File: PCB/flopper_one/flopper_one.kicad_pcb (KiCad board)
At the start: 2 copper layers, 77 x 63 mm, 21 parts, among them J1 To PN532 ->, J2 <- ST7789, Q1 2N2219, SW1 SW_Omron_B3FS, SW2 SW_Omron_B3FS, SW3 SW_Omron_B3FS, SW4 SW_Omron_B3FS, SW5 SW_Omron_B3FS, U1 TP4056-42-ESOP8, U4 hw-045

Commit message: clean stuff up
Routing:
- net GND: track 332.5 -> 362.7 mm, vias 1 -> 0
- net /BAT+: track 33.6 -> 25.7 mm
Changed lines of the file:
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@@
 		(at 169.805 107.7 -90)
 		(property "Reference" "U2"
-			(at -11.355 -27.36 90)
+			(at 0 0 180)
 			(layer "F.SilkS")
 			(effects
@@
 	)
 	(gr_rect
-		(start 197.375 81.3125)
-		(end 199.625 83.6875)
+		(start 197.5 81.25)
+		(end 199.75 83.75)
 		(stroke
-			(width 0.1)
+			(width 0.2)
 			(type solid)
 		)
 		(fill yes)
 		(layer "B.Cu")
+		(net 3)
+	)
+	(gr_rect
+		(start 193.125 81.25)
+		(end 195.375 83.625)
+		(stroke
+			(width 0.2)
+			(type default)
+		)
+		(fill no)
+		(layer "B.Cu")
 		(net 39)
 	)
@@
 	)
 	(gr_text "ESP HERE"
-		(at 164 105 0)
+		(at 165.25 105 0)
 		(layer "F.SilkS")
 		(effects
@@
 	)
 	(segment
+		(start 192.75 106)
+		(end 196.375 102.375)
+		(width 0.2)
+		(layer "F.Cu")
+		(net 3)
+	)
+	(segment
 		(start 202.865 95.19)
 		(end 204.075 95.19)
@@
 	)
 	(segment
-		(start 197.25 103.25)
+		(start 196.375 102.375)
 		(end 192 98)
 		(width 0.2)
@@
 	)
 	(segment
+		(start 196.5 102.5)
+		(end 196.375 102.375)
+		(width 0.2)
+		(layer "F.Cu")
+		(net 3)
+	)
+	(segment
 		(start 209 63)
 		(end 208 62)
@@
 	)
 	(segment
-		(start 205 81)
-		(end 204.25 81)
+		(start 196.5 102.5)
+		(end 197.38 102.5)
 		(width 0.2)
 		(layer "F.Cu")
@@
 	)
 	(segment
-		(start 206 89.25)
-		(end 208 87.25)
+		(start 197.38 102.5)
+		(end 197.69 102.81)
+		(width 0.2)
+		(layer "F.Cu")
+		(net 3)
+	)
+	(segment
+		(start 205 81)
+		(end 204.25 81)
 		(width 0.2)
 		(layer "F.Cu")
@@
 	)
 	(segment
-		(start 195.5 103.25)
-		(end 197.25 103.25)
+		(start 206 89.25)
+		(end 208 87.25)
 		(width 0.2)
 		(layer "F.Cu")
@@
 	)
 	(segment
-		(start 206 89.25)
-		(end 206 87.75)
-		(width 0.2)
-		(layer "F.Cu")
-		(net 3)
-	)
-	(segment
 		(start 200.9 97.025)
 		(end 202.3 97.025)
@@
 	)
 	(segment
-		(start 197.25 103.25)
-		(end 197.69 102.81)
-		(width 0.2)
-		(layer "F.Cu")
-		(net 3)
-	)
-	(segment
 		(start 149.221108 121.701)
 		(end 148.459 120.938892)
@@
 	)
 	(segment
-		(start 192.75 106)
-		(end 195.5 103.25)
-		(width 0.2)
-		(layer "F.Cu")
-		(net 3)
-	)
-	(segment
 		(start 152.3 120.4)
 		(end 150.999 121.701)
@@
 		(net 3)
 	)
-	(via
-		(at 206 87.75)
-		(size 0.6)
-		(drill 0.3)
-		(layers "F.Cu" "B.Cu")
+	(segment
+		(start 208.05 88.75)
+		(end 204.899 91.901)
+		(width 0.2)
+		(layer "B.Cu")
 		(net 3)
 	)
@@
 	)
 	(segment
+		(start 211.210057 102.81)
+		(end 216.25 102.81)
+		(width 0.2)
+		(layer "B.Cu")
+		(net 3)
+	)
+	(segment
+		(start 204.899 96.498943)
+		(end 211.210057 102.81)
+		(width 0.2)
+		(layer "B.Cu")
+		(net 3)
+	)
+	(segment
 		(start 215.71 117.79)
 		(end 214 119.5)
@@
 	)
 	(segment
+		(start 204.899 91.901)
+		(end 204.899 96.498943)
+		(width 0.2)
+		(layer "B.Cu")
+		(net 3)
+	)
+	(segment
 		(start 208.15 119.5)
 		(end 214 119.5)
@@
 	)
 	(segment
-		(start 184.52324 72.691)
-		(end 185.47676 72.691)
+		(start 208.05 88.75)
+		(end 201.8 82.5)
 		(width 0.2)
 		(layer "B.Cu")
@@
 	)
 	(segment
-		(start 185 97.22)
-		(end 185 98)
+		(start 201.8 82.5)
+		(end 198.625 82.5)
+		(width 0.2)
+		(layer "B.Cu")
+		(net 3)
+	)
+	(segment
+		(start 184.52324 72.691)
+		(end 185.47676 72.691)
 		(width 0.2)
 		(layer "B.Cu")
@@
 	)
 	(segment
-		(start 207.05 87.75)
-		(end 208.05 88.75)
+		(start 185 97.22)
+		(end 185 98)
 		(width 0.2)
 		(layer "B.Cu")
@@
 	)
 	(segment
-		(start 206 87.75)
-		(end 207.05 87.75)
-		(width 0.2)
-		(layer "B.Cu")
-		(net 3)
-	)
-	(segment
 		(start 152.04 71.065)
 		(end 152.04 67.5271)
@@
 	)
 	(segment
-		(start 198.5 82.5)
-		(end 198.5 83)
-		(width 0.2)
-		(layer "B.Cu")
-		(net 39)
-	)
-	(segment
 		(start 199.499999 93)
 		(end 201.25 91.249999)
@@
 	)
 	(segment
-		(start 201.25 88.75)
-		(end 201.25 85.25)
-		(width 0.2)
-		(layer "B.Cu")
-		(net 39)
-	)
-	(segment
 		(start 197.5 93)
 		(end 199.499999 93)
 		(width 0.2)
 		(layer "B.Cu")
-		(net 39)
-	)
-	(segment
-		(start 201.25 85.25)
-		(end 198.5 82.5)
-		(width 0.2)
-		(layer "B.Cu")

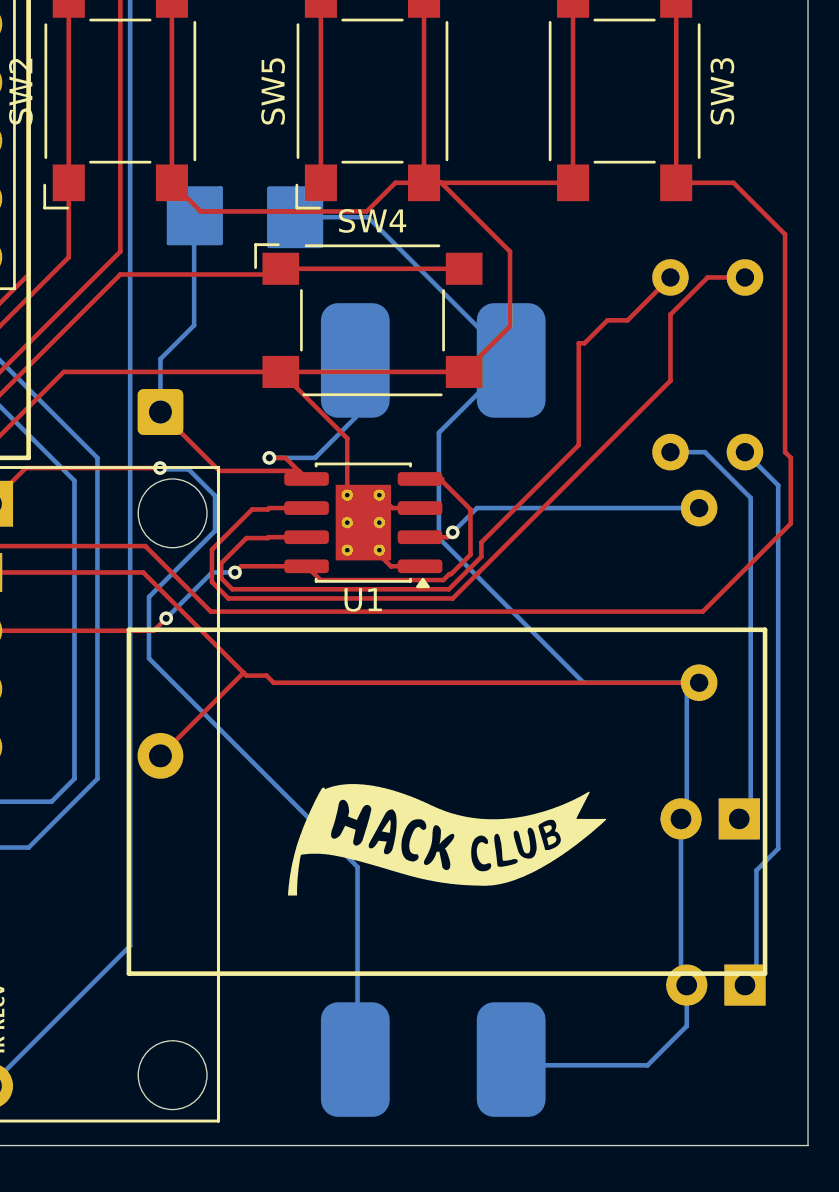
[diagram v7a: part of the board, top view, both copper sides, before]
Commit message: add nice 3d models
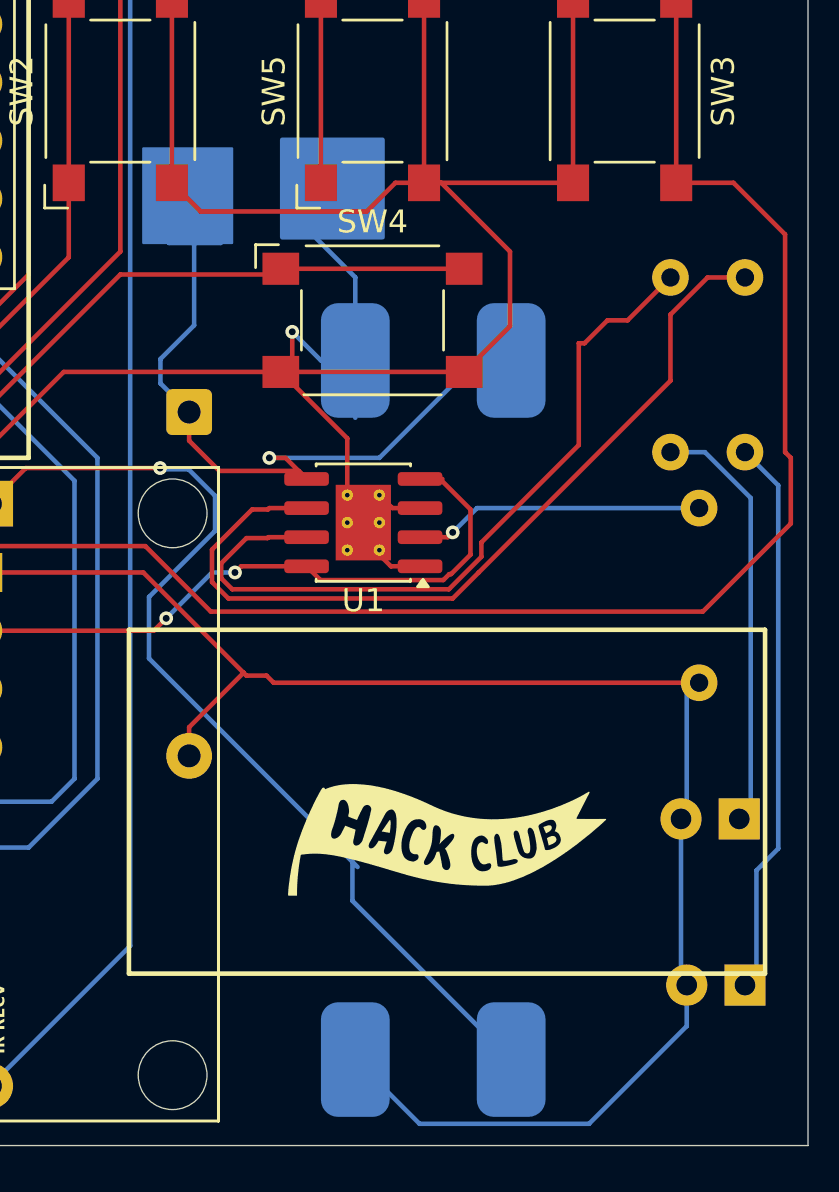
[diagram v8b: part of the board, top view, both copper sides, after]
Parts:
- moved C1 1.25 mm to (194.0, 91.0)
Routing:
- net GND: track 362.7 -> 351.3 mm, vias 0 -> 1
- net /BAT+: track 25.7 -> 31.1 mm
- net /VIN: track 40.8 -> 43.6 mm
